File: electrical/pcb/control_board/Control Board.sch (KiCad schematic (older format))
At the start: 104 parts, among them J1 ED2627-ND, J10 6posheader, J11 S7038-ND, J13 ED1501-ND, J14 ED2989-ND-USB, J15 ED2580-ND, J16 ED2580-ND, J17 ED2744-ND, J18 ED2744-ND, J19 ED2744-ND, J2 ED2627-ND, J20 ED2744-ND, J21 ED2744-ND, J22 ED2744-ND, J23 ED2744-ND, J24 ED2744-ND, J25 ED2744-ND, J26 ED2744-ND, J28 ED2580-ND, J29 ED2580-ND, J3 ED2627-ND, J30 ED2580-ND, J31 ED2580-ND, J4 ED2627-ND, J5 ED2627-ND, J6 S9175-ND, J7 S9175-ND, J8 6posheader, J9 S7038-ND, M1 Mounting_Holes, T1 test_point, T10 test_point, T11 test_point, T12 test_point, T13 test_point, T14 test_point, T15 test_point, T16 test_point, T17 test_point, T18 test_point, T19 test_point, T2 test_point, T20 test_point, T21 test_point, T3 test_point, T4 test_point, T5 test_point, T6 test_point, T7 test_point, T8 test_point, T9 test_point, U1 LM358-N, U2 LM358-N, y1 rover_silkscreen

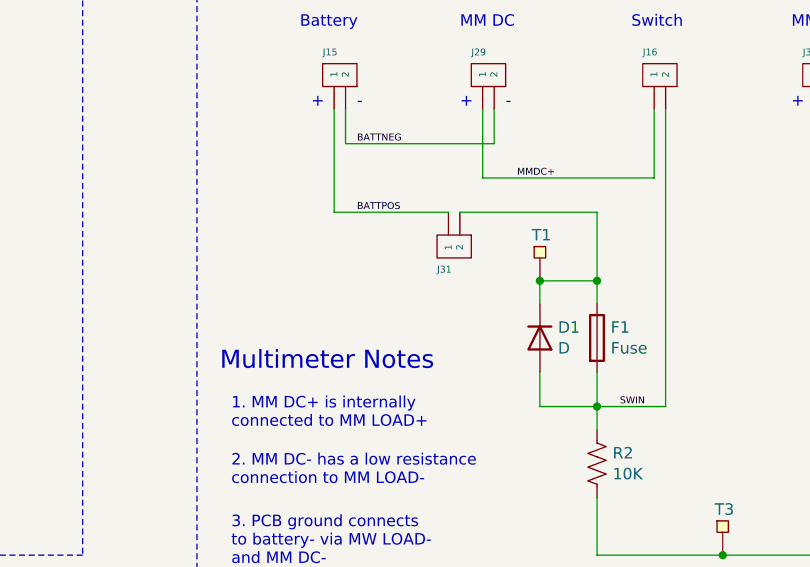
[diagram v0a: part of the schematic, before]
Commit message: updating get ignore to ignore kicad bak files, and adding a note by j31 about ina260 sensor
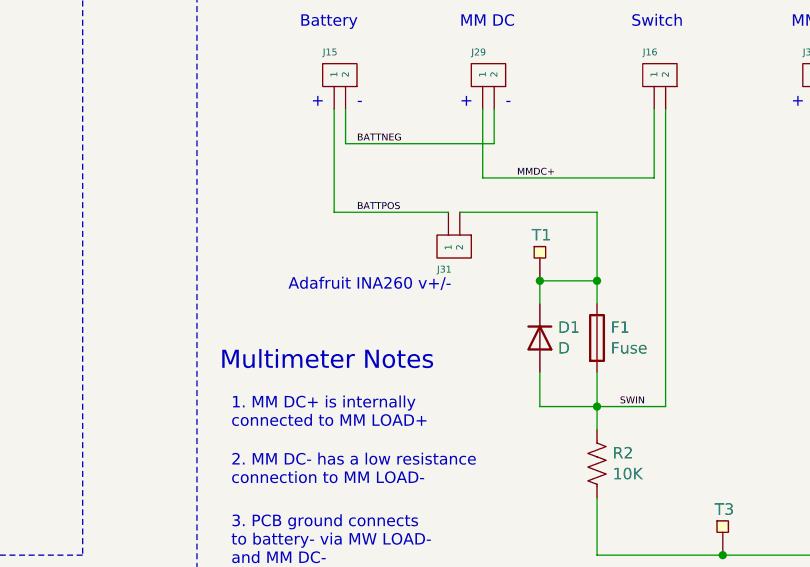
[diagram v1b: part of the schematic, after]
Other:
- note added: "Adafruit INA260 v+/-"
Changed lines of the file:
@@
 Text Label 14500 3550 0    30   ~ 0
 RC3EN2B
+Text Notes 4250 6900 0    50   ~ 0
+Adafruit INA260 v+/-
 $EndSCHEMATC

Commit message: updating all the symbol library references in the control board schematic. Now everything should just refer to the jpl robotics library, and not any of the cache or rescue files
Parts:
- J1, J2, J3, J4, J5: symbol Control-Board-rescue:ED2627-ND-JPL_Robotics_Lib-Monolithic-Board-rescue -> JPL_Robotics_Lib:ED2627-ND
- J10, J8: symbol Control-Board-rescue:6posheader-JPL_Robotics_Lib-Monolithic-Board-rescue -> JPL_Robotics_Lib:6posheader
- J11, J9: symbol Control-Board-rescue:S7038-ND-JPL_Robotics_Lib-Monolithic-Board-rescue -> JPL_Robotics_Lib:S7038-ND
- J13: symbol Control-Board-rescue:ED1501-ND-JPL_Robotics_Lib-Monolithic-Board-rescue -> JPL_Robotics_Lib:ED1501-ND
- J14: symbol Control-Board-rescue:ED2989-ND-USB-JPL_Robotics_Lib-Monolithic-Board-rescue -> JPL_Robotics_Lib:ED2989-ND-USB
- J15, J16, J28, J29, J30, J31: symbol Control-Board-rescue:ED2580-ND-JPL_Robotics_Lib-Monolithic-Board-rescue -> JPL_Robotics_Lib:ED2580-ND
- J17, J18, J19, J20, J21, J22, J23, J24, J25, J26: symbol Control-Board-rescue:ED2744-ND-JPL_Robotics_Lib-Monolithic-Board-rescue -> JPL_Robotics_Lib:ED2744-ND
- J6, J7: symbol Control-Board-rescue:S9175-ND-JPL_Robotics_Lib-Monolithic-Board-rescue -> JPL_Robotics_Lib:S9175-ND
- M1: symbol Control-Board-rescue:Mounting_Holes-JPL_Robotics_Lib-Monolithic-Board-rescue -> JPL_Robotics_Lib:Mounting_Holes
- MH1, MH2, MH3, MH4: symbol Control-Board-rescue:#6THRU-HOLE-JPL_Robotics_Lib-Monolithic-Board-rescue -> JPL_Robotics_Lib:#6THRU-HOLE
- RC1, RC2, RC3, RC4, RC5: symbol Control-Board-rescue:RoboClaw-JPL_Robotics_Lib-Monolithic-Board-rescue -> JPL_Robotics_Lib:RoboClaw
- T1, T10, T11, T12, T13, T14, T15, T16, T17, T18, T19, T2, T20, T21, T3, T4, T5, T6, T7, T8, T9: symbol Control-Board-rescue:test_point-JPL_Robotics_Lib-Monolithic-Board-rescue -> JPL_Robotics_Lib:test_point
- U1, U2: symbol Control-Board-rescue:LM358-N-JPL_Robotics_Lib-Monolithic-Board-rescue -> JPL_Robotics_Lib:LM358-N
- y1: symbol Control-Board-rescue:rover_silkscreen-Monolithic-Board-rescue -> JPL_Robotics_Lib:rover_silkscreen

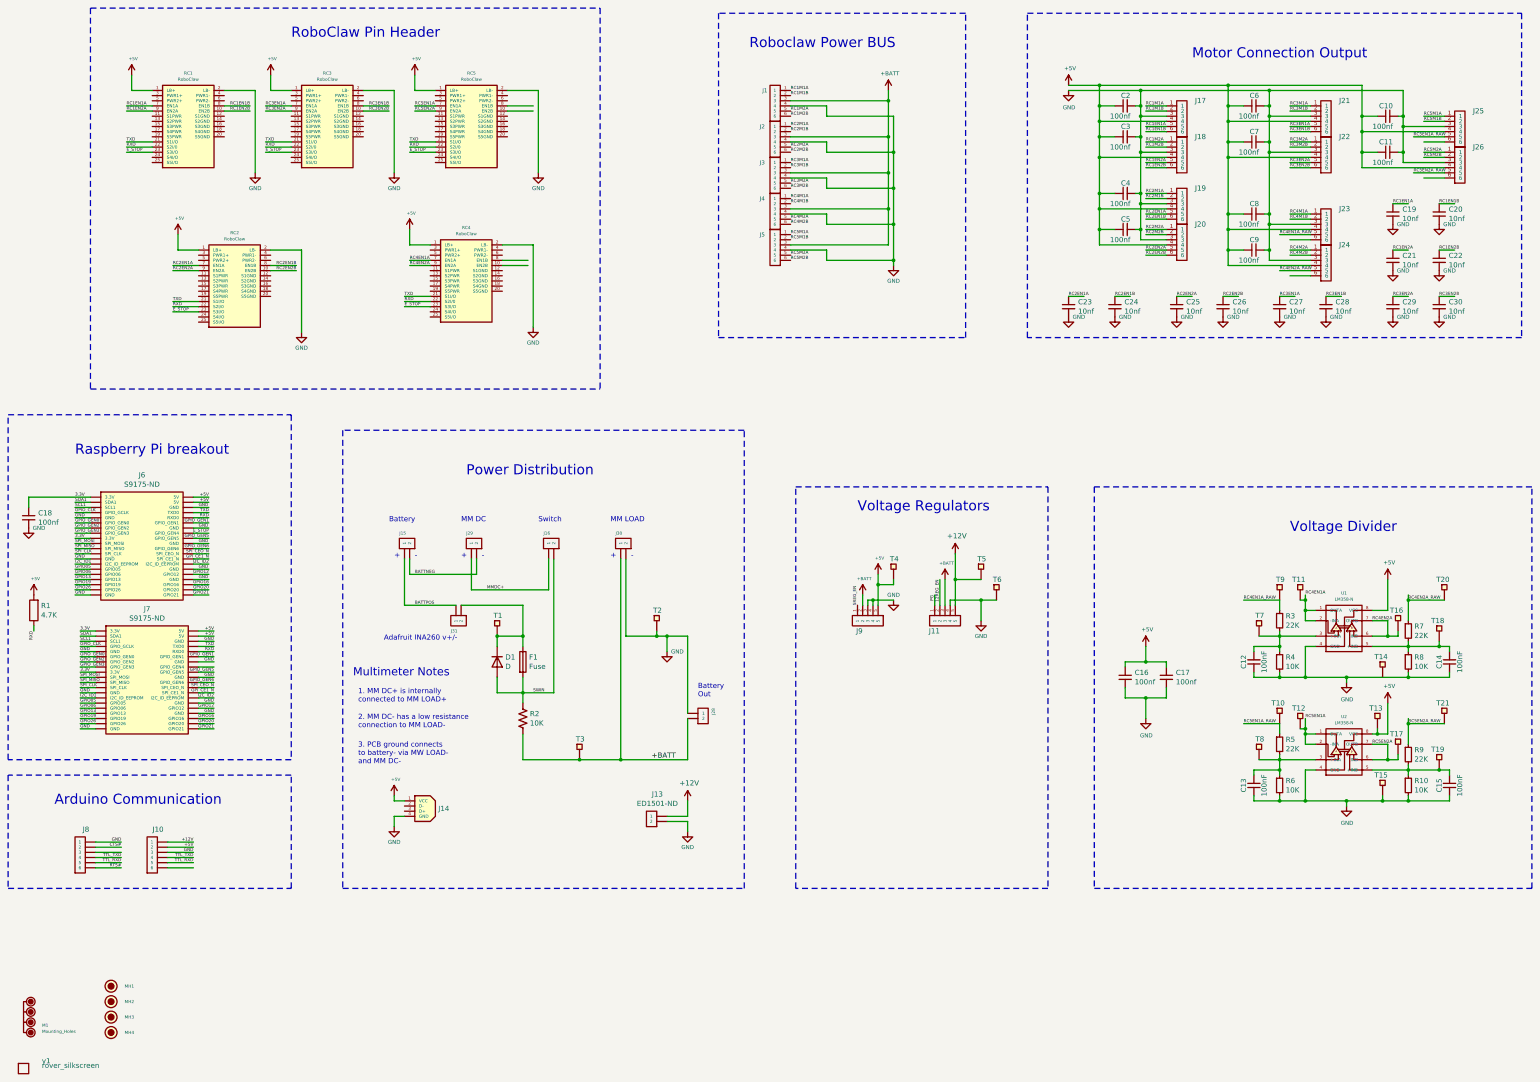
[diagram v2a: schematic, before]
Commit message: making progress on updates to pin definitions in symbol library
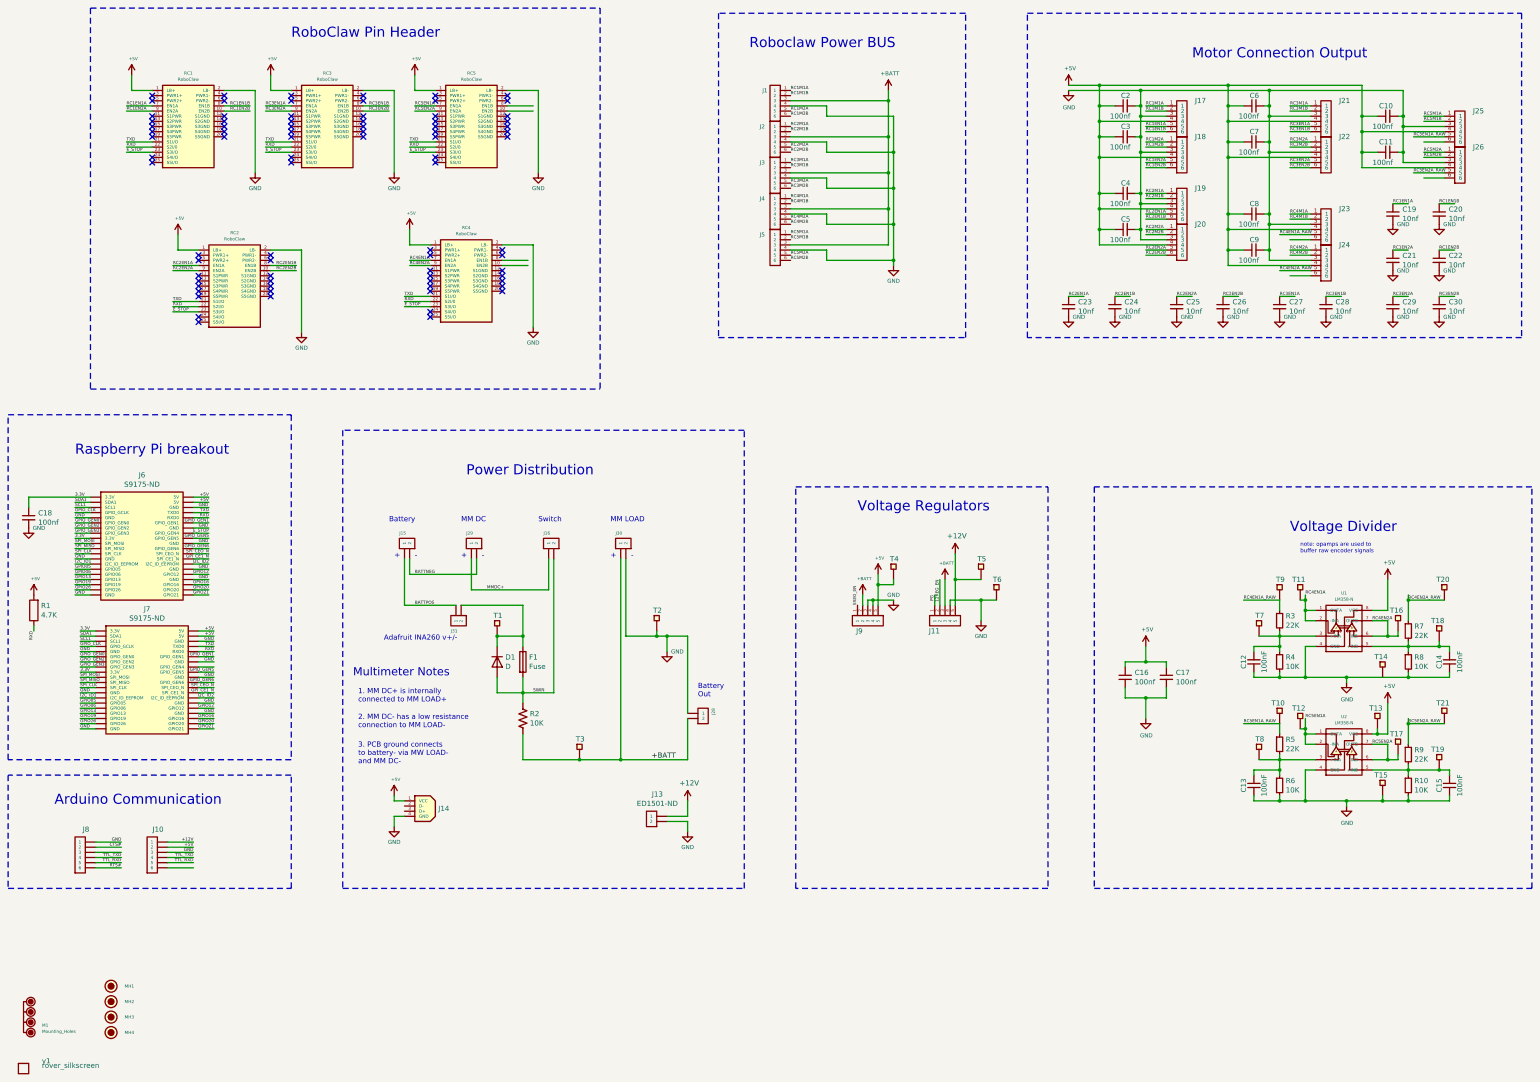
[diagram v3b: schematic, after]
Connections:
- no-connect marks 0 -> 80
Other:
- note added: "note: opamps are used to \nbuffer raw encoder signals"
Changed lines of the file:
@@
 Text Notes 4250 6900 0    50   ~ 0
 Adafruit INA260 v+/-
+Text Notes 13150 6050 0    39   ~ 0
+note: opamps are used to \nbuffer raw encoder signals
+NoConn ~ 2000 1600
+NoConn ~ 2000 1650
+NoConn ~ 2700 1600
+NoConn ~ 2700 1650
+NoConn ~ 2700 1800
+NoConn ~ 2700 1850
+NoConn ~ 2700 1900
+NoConn ~ 2700 1950
+NoConn ~ 2700 2000
+NoConn ~ 2000 1800
+NoConn ~ 2000 1850
+NoConn ~ 2000 1900
+NoConn ~ 2000 1950
+NoConn ~ 2000 2000
+NoConn ~ 2000 2200
+NoConn ~ 2000 2250
+NoConn ~ 3350 1600
+NoConn ~ 3350 1650
+NoConn ~ 3350 1800
+NoConn ~ 3350 1850
+NoConn ~ 3350 1900
+NoConn ~ 3350 1950
+NoConn ~ 3350 2000
+NoConn ~ 3350 2200
+NoConn ~ 3350 2250
+NoConn ~ 4050 1600
+NoConn ~ 4050 1650
+NoConn ~ 4050 1800
+NoConn ~ 4050 1850
+NoConn ~ 4050 1900
+NoConn ~ 4050 1950
+NoConn ~ 4050 2000
+NoConn ~ 4750 1600
+NoConn ~ 4750 1650
+NoConn ~ 4750 1800
+NoConn ~ 4750 1850
+NoConn ~ 4750 1900
+NoConn ~ 4750 1950
+NoConn ~ 4750 2000
+NoConn ~ 4750 2200
+NoConn ~ 4750 2250
+NoConn ~ 5450 1600
+NoConn ~ 5450 1650
+NoConn ~ 5450 1800
+NoConn ~ 5450 1850
+NoConn ~ 5450 1900
+NoConn ~ 5450 1950
+NoConn ~ 5450 2000
+NoConn ~ 2450 3150
+NoConn ~ 2450 3200
+NoConn ~ 2450 3350
+NoConn ~ 2450 3400
+NoConn ~ 2450 3450
+NoConn ~ 2450 3500
+NoConn ~ 2450 3550
+NoConn ~ 2450 3750
+NoConn ~ 2450 3800
+NoConn ~ 3150 3150
+NoConn ~ 3150 3200
+NoConn ~ 3150 3350
+NoConn ~ 3150 3400
+NoConn ~ 3150 3450
+NoConn ~ 3150 3500
+NoConn ~ 3150 3550
+NoConn ~ 4700 3100
+NoConn ~ 4700 3150
+NoConn ~ 4700 3300
+NoConn ~ 4700 3350
+NoConn ~ 4700 3400
+NoConn ~ 4700 3450
+NoConn ~ 4700 3500
+NoConn ~ 4700 3700
+NoConn ~ 4700 3750
+NoConn ~ 5400 3100
+NoConn ~ 5400 3150
+NoConn ~ 5400 3300
+NoConn ~ 5400 3350
+NoConn ~ 5400 3400
+NoConn ~ 5400 3450
+NoConn ~ 5400 3500
 $EndSCHEMATC

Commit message: Got the control board schematic passing electrical rules check in kicad
This took a fair bit of finagling with the components in the library.
See notes in the readme.md in the control board directory
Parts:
- J11: symbol JPL_Robotics_Lib:S7038-ND -> JPL_Robotics_Lib:S7038-ND_regulator_D24V22F12
- J6, J7: value S9175-ND -> S9175-ND_rpi_breakout; symbol JPL_Robotics_Lib:S9175-ND -> JPL_Robotics_Lib:S9175-ND_rpi_breakout
- J9: symbol JPL_Robotics_Lib:S7038-ND -> JPL_Robotics_Lib:S7038-ND_regulator_D24V50F5
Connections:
- net labels removed: 12REG_EN, 5REG_EN, GPIO05, GPIO06, GPIO12, GPIO13, GPIO16, GPIO19, GPIO20, GPIO21, GPIO26, GPIO_CLK, GPIO_GEN0, GPIO_GEN1, GPIO_GEN2, GPIO_GEN3, GPIO_GEN5, GPIO_GEN6, GPI_CE1_N, I2C_ID1, I2C_ID2, PG, SCL1, SDA1, SPI_CEO_N, SPI_CLK, SPI_MISO, SPI_MOSI
- wire segments 477 -> 421
- no-connect marks 80 -> 149
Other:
- note added: "*3.3v bus is \nnot powered"
- moved on the sheet: J11, J13, J9, T14, T5
